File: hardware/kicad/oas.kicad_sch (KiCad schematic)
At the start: 0 parts

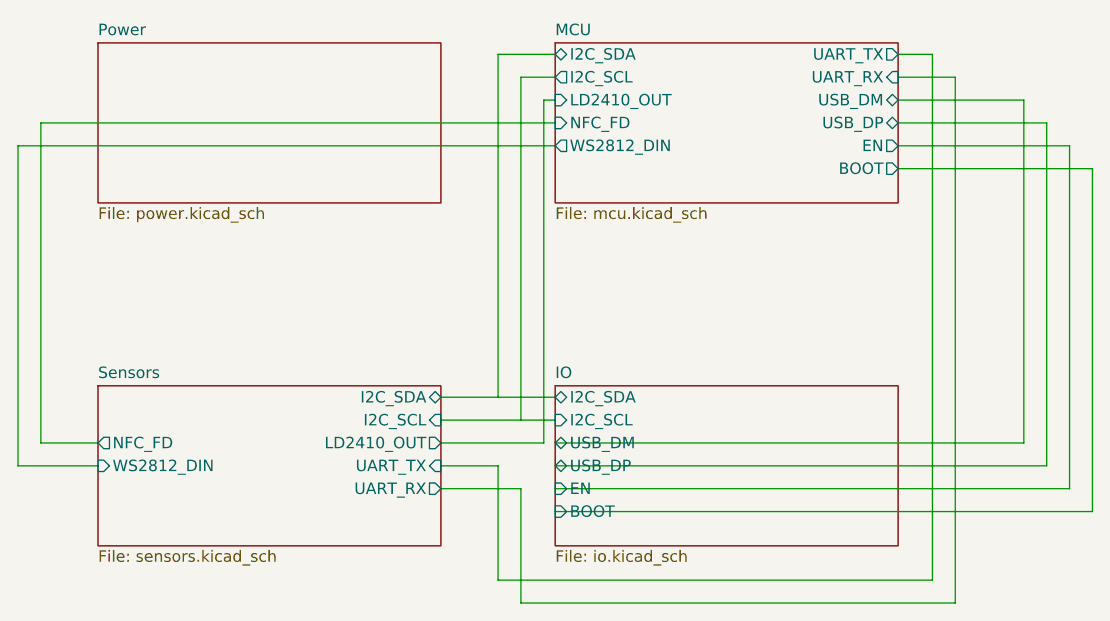
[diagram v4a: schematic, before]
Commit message: feat(sw1): add SW1 side-actuated tactile push-button (v0.42)
Adds the C&K PTS645VK392LFS right-angle THT push-button on ESP32-C6
GPIO 1, mounted in the AK-N-94 USB-C case-wall opening. Short press
cycles the LED ring brightness, long press restarts the MCU.

Hardware: GPIO 1 -> BTN net, new USBC cutout + SW1 placement constants,
Switch:SW_Push stock symbol on the IO sheet, verbatim-stock PTS645
footprint, inter-sheet BTN wiring (IO -> MCU). SW1 added to
THT_REFERENCES; DRC EXPECTED_UNCONNECTED 88 -> 89 (BTN ratsnest routed
in the pending routing rework).

Firmware: new packages/buttons.yaml (GPIO1 binary_sensor + brightness-
cycle script), wired into oas.yaml.

All 29 pipeline stages PASS; boardgen output deterministic.

Co-Authored-By: Claude Opus 4.7 <noreply@anthropic.com>
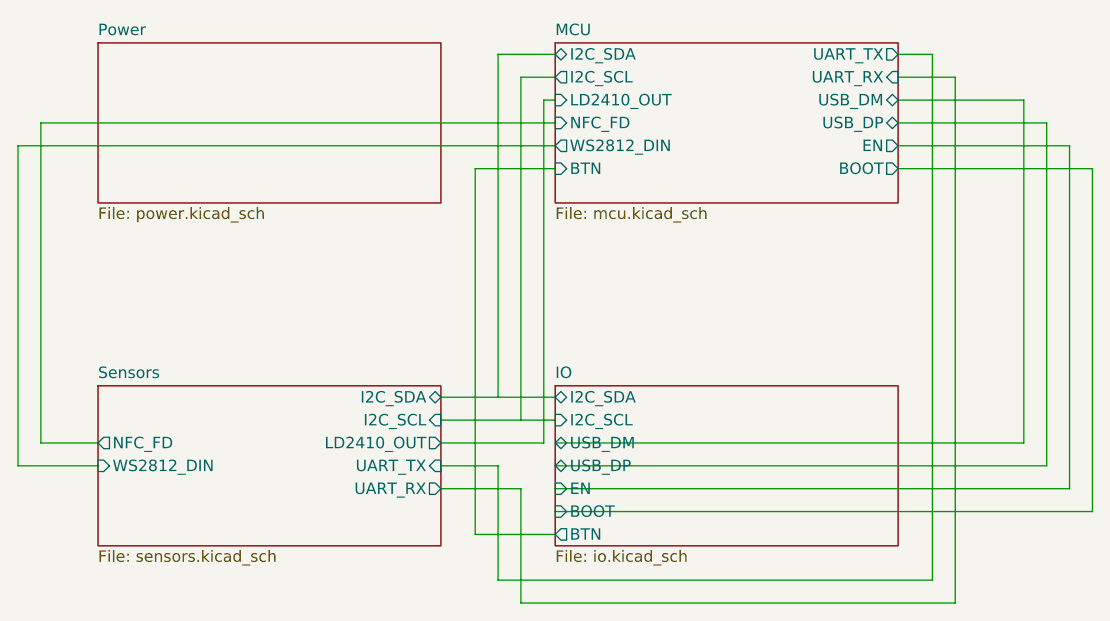
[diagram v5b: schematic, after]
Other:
- sheet IO ports: added BTN; removed none
- sheet MCU ports: added BTN; removed none
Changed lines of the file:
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@@
+			)
+		)
+		(pin "BTN" input
+			(at 101.6 64.77 180)
+			(effects
+				(font
+					(size 1.27 1.27)
+				)
+				(justify right)
 			)
 		)
@@
 			)
 		)
+		(pin "BTN" output
+			(at 101.6 105.41 180)
+			(effects
+				(font
+					(size 1.27 1.27)
+				)
+				(justify right)
+			)
+		)
 		(instances
 			(project "oas"
@@
 	)
 	(stroke
+		(width 0)
+		(type default)
+	)
+)
+(wire
+	(pts
+		(xy 101.6 64.77) (xy 92.71 64.77)
+	)
+	(stroke
+		(width 0)
+		(type default)
+	)
+)
+(wire
+	(pts
+		(xy 92.71 64.77) (xy 92.71 105.41)
+	)
+	(stroke
+		(width 0)
+		(type default)
+	)
+)
+(wire
+	(pts
+		(xy 92.71 105.41) (xy 101.6 105.41)
+	)
+	(stroke

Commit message: hardware+firmware: remove the SW1 user push-button
Closes #5.

- boardgen: drop SW1 (C&K PTS645VK392LFS) from the IO schematic sheet,
  PCB placement, footprint emitters and Z-clearance entries; GPIO1
  (J5.8) becomes a spare no_connect and joins GPIO_SPARE (9 spares).
  The AK-N-94 USB-C case-wall opening annotation stays (enclosure
  feature) but no longer hosts a component.
- routing snapshot: remove the 9 /IO/BTN records, canonical re-extract
  renumbers uuid_tags -> 606 segments + 40 vias (was 613 + 42);
  test_project_constants + test_extract_routes counts updated.
- pipeline: SW1 out of THT_REFERENCES and the silk-strip special cases.
- firmware: delete packages/buttons.yaml and its include from oas.yaml
  (7 -> 6 packages); README updated.
- docs: CLAUDE.md module list, GPIO pinout table, spare-GPIO list,
  THT hand-solder TODO, repo-layout package list.

build.py 35/35 PASS; DRC 0 violations / 0 unconnected; ERC 0/0.

Co-Authored-By: Claude Fable 5 <noreply@anthropic.com>
Claude-Session: https://claude.ai/code/session_017QqgHNrNySNTKB44F1FsEB
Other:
- sheet IO ports: added none; removed BTN
- sheet MCU ports: added none; removed BTN
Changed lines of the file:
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@@
-			)
-		)
-		(pin "BTN" input
-			(at 101.6 64.77 180)
-			(effects
-				(font
-					(size 1.27 1.27)
-				)
-				(justify right)
 			)
 		)
@@
 			)
 		)
-		(pin "BTN" output
-			(at 101.6 105.41 180)
-			(effects
-				(font
-					(size 1.27 1.27)
-				)
-				(justify right)
-			)
-		)
 		(instances
 			(project "oas"
@@
 	)
 	(stroke
-		(width 0)
-		(type default)
-	)
-)
-(wire
-	(pts
-		(xy 101.6 64.77) (xy 92.71 64.77)
-	)
-	(stroke
-		(width 0)
-		(type default)
-	)
-)
-(wire
-	(pts
-		(xy 92.71 64.77) (xy 92.71 105.41)
-	)
-	(stroke
-		(width 0)
-		(type default)
-	)
-)
-(wire
-	(pts
-		(xy 92.71 105.41) (xy 101.6 105.41)
-	)
-	(stroke

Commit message: hardware+firmware: remove the dynamic NFC tag (MIKROE-2462 / NT3H1101)
Closes #7.

The NFC feature is dropped entirely: RF coupling through the AK-N-94
cover is unusable as integrated, the only workable fix (cover-mounted
antenna) breaks the aesthetic pillar, and the LED ring + HA dashboard
already cover the need. Recorded in CLAUDE.md Out-of-scope.

Hardware (boardgen):
- MOD2 (oas:MIKROE-2462_Reference), J7 + J8 mikroBUS sockets and C12
  decoupling removed from schematic, placement, footprints, Z-clearance
  and the stage-18 whitelist (9 -> 8 documented customs).
- GPIO 3 (net NFC_FD) freed -> spare no_connect, same pattern as GPIO 1
  in the SW1 removal; ten spare safe-non-strap GPIOs now.
- Routing snapshot 600 seg + 40 via -> 586 seg + 43 via: /MCU/NFC_FD
  (2 seg) and 12 dead GND stitches anchored at the removed pads swept;
  3 bridge vias added where former J7.7/J8.5/J8.6 THT pads carried the
  live +3V3 / I2C_SCL / I2C_SDA layer transitions feeding the SEN66
  (J3). Clearance at the via spots >= 0.71 mm vs the 0.20 mm rule.
- I2C bus is now SEN66 + Qwiic; stage 26 rise time improves to
  278/277 ns (was 306/305) vs the 1000 ns Standard-mode ceiling.
- POWER_BUDGET, EXTERNAL_MODULES, THT_REFERENCES, tests and BOM/CPL
  deliverables updated; dead 2x8-connector schematic helper removed.

Firmware (esphome):
- packages/nfc.yaml deleted; dashboard_url substitution and all NFC
  references removed from oas.yaml, package comments and READMEs.
- HARDWARE-COMPAT-v0.51.md: removal recorded as final; the five v0.51
  boards keep unpopulated J7/J8/MOD2 footprints.

Verification: implemented and adversarially reviewed by two independent
agents; build.py 35/35 PASS on both runs; DRC 0 violations /
0 unconnected; ERC 0/0; F.Cu pour refills the former mikroBUS field
with no orphan islands; deliverables (BOM/CPL/gerbers/ibom) carry zero
NFC references.

Co-Authored-By: Claude Fable 5 <noreply@anthropic.com>
Claude-Session: https://claude.ai/code/session_017QqgHNrNySNTKB44F1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
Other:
- sheet MCU ports: added none; removed NFC_FD
- sheet Sensors ports: added none; removed NFC_FD
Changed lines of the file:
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@@
-			)
-		)
-		(pin "NFC_FD" input
-			(at 101.6 59.69 180)
-			(effects
-				(font
-					(size 1.27 1.27)
-				)
-				(justify right)
 			)
 		)
@@
 			)
 		)
-		(pin "NFC_FD" output
-			(at 50.8 95.25 180)
-			(effects
-				(font
-					(size 1.27 1.27)
-				)
-				(justify right)
-			)
-		)
 		(pin "WS2812_DIN" input
 			(at 50.8 97.79 180)
@@
 	)
 	(stroke
-		(width 0)
-		(type default)
-	)
-)
-(wire
-	(pts
-		(xy 50.8 95.25) (xy 44.45 95.25)
-	)
-	(stroke
-		(width 0)
-		(type default)
-	)
-)
-(wire
-	(pts
-		(xy 44.45 95.25) (xy 44.45 59.69)
-	)
-	(stroke
-		(width 0)
-		(type default)
-	)
-)
-(wire
-	(pts
-		(xy 44.45 59.69) (xy 101.6 59.69)
-	)
-	(stroke

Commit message: hardware+firmware: move the LD2410 UART off GPIO16/17 (CP2102N contention)
The LD2410 UART sat on GPIO16/17 from v0.4 on the reasoning that those are
"just the default UART0 pins" and the C6's GPIO matrix can re-route UART0.
That reasoning covers the SoC only. On the ESP32-C6-DevKitM-1 the same two
pads are wired through populated 0 R links (R9 -> CP2102N RXD pin 25,
R7 -> CP2102N TXD pin 26) to the onboard USB-UART bridge, and that bridge's
VDD (6) + REGIN (7) tie to VCC_3V3 -- the board rail OAS drives at J5.1 --
not to USB VBUS (pin 8 only sees the R19/R18 sense divider). So the bridge
is powered whenever the unit is, and its TXD is a push-pull output parked
on the ESP's RX net. Two drivers, one node.

Bench-proved on a v0.51 board with the radar unpowered (24 V off) and the
bridge's own USB port empty, probing with the ESP's internal pulls:
  GPIO2  pu=1/pd=0  FLOATING
  GPIO16 pu=1/pd=0  FLOATING
  GPIO17 pu=1/pd=1  DRIVEN
The two control pins follow the pulls; GPIO17 holds HIGH against its own
pull-down with nothing on that net but the bridge's TXD.

Fix: the pair moves to GPIO 1 (TX) / GPIO 0 (RX) -- free, adjacent,
non-strap pads on J5, the socket row nearest J4. Nets renamed
LD2410_UART_TX / LD2410_UART_RX; UART_TX / UART_RX stay as the true console
on GPIO16/17, reaching only the DNP recovery header J2 (that header exists
to serial-flash a module whose USB ports are dead, so it belongs on the ROM
bootloader's own pins and must not follow a peripheral around).

GPIO16/17 move into GPIO_RESERVED, and stage 06 grows a console-pin check
that fails if any refdes other than J6/J2 appears on either console net --
a dict entry is a comment, a check is a guarantee.

Replacement pins vetted the same way the old ones failed: GPIO0/1 double as
XTAL_32K_P/N and the DevKitM-1 does carry that network, but Y1, C4/C5 and
R1 are all (NC) on the Espressif schematic and only the 0 R links R3/R2 to
the header are populated -- the pads are electrically bare.

Firmware gains ld2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
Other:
- sheet MCU ports: added LD2410_UART_RX, LD2410_UART_TX; removed UART_RX, UART_TX
- sheet Sensors ports: added LD2410_UART_RX, LD2410_UART_TX; removed UART_RX, UART_TX
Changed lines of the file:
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@@
 			)
 		)
-		(pin "UART_TX" output
+		(pin "LD2410_UART_TX" output
 			(at 139.7 52.07 0)
 			(effects
@@
 			)
 		)
-		(pin "UART_RX" input
+		(pin "LD2410_UART_RX" input
 			(at 139.7 54.61 0)
 			(effects
@@
 			)
 		)
-		(pin "UART_TX" input
+		(pin "LD2410_UART_TX" input
 			(at 88.9 97.79 0)
 			(effects
@@
 			)
 		)
-		(pin "UART_RX" output
+		(pin "LD2410_UART_RX" output
 			(at 88.9 100.33 0)
 			(effects
